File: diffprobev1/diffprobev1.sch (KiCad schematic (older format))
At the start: 36 parts

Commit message: diffprobe sch
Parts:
- added J? (x3): Conn_01x02_Male, symbol Connector:Conn_01x02_Male
- added J? (x2): Conn_01x03_Male, symbol Connector:Conn_01x03_Male
- added unit 3 of U1
- U?: value LF356 -> TL072
- U?: value TL082 -> TL072
- gave numbers to parts that had none: 1
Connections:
- wire segments 0 -> 91
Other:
- moved on the sheet: C?, D?, R?, U1A, U?

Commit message: almost there
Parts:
- removed C? (x2): C, symbol Device:C
- removed C?: CP, symbol Device:CP
- removed J?: Conn_01x02_Male, symbol Connector:Conn_01x02_Male
- removed J?: Conn_01x03_Male, symbol Connector:Conn_01x03_Male
- removed Q?: Q_PNP_EBC, symbol Device:Q_PNP_EBC
- removed R? (x6): R, symbol Device:R
- removed U?: TL072, symbol Amplifier_Operational:LF356
- removed U?: TL072, symbol Amplifier_Operational:TL082
- added C? (x18): C, symbol Device:C
- added C? (x5): CP, symbol Device:CP
- added D? (x4): D_Zener, symbol Device:D_Zener
- added D? (x12): D, symbol Device:D
- added J? (x7): Conn_01x02_Male, symbol Connector:Conn_01x02_Male
- added J?: 8P8C, symbol Connector:8P8C
- added R? (x32): R, symbol Device:R
- added U? (x3): TL071, symbol Amplifier_Operational:TL071
- added U? (x6): TL072, symbol Amplifier_Operational:TL072
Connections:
- net labels added: +15V, -15V, GND1
- wire segments 91 -> 416
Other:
- moved on the sheet: C?, D?, J?, R?, U1A, U1B, U1C

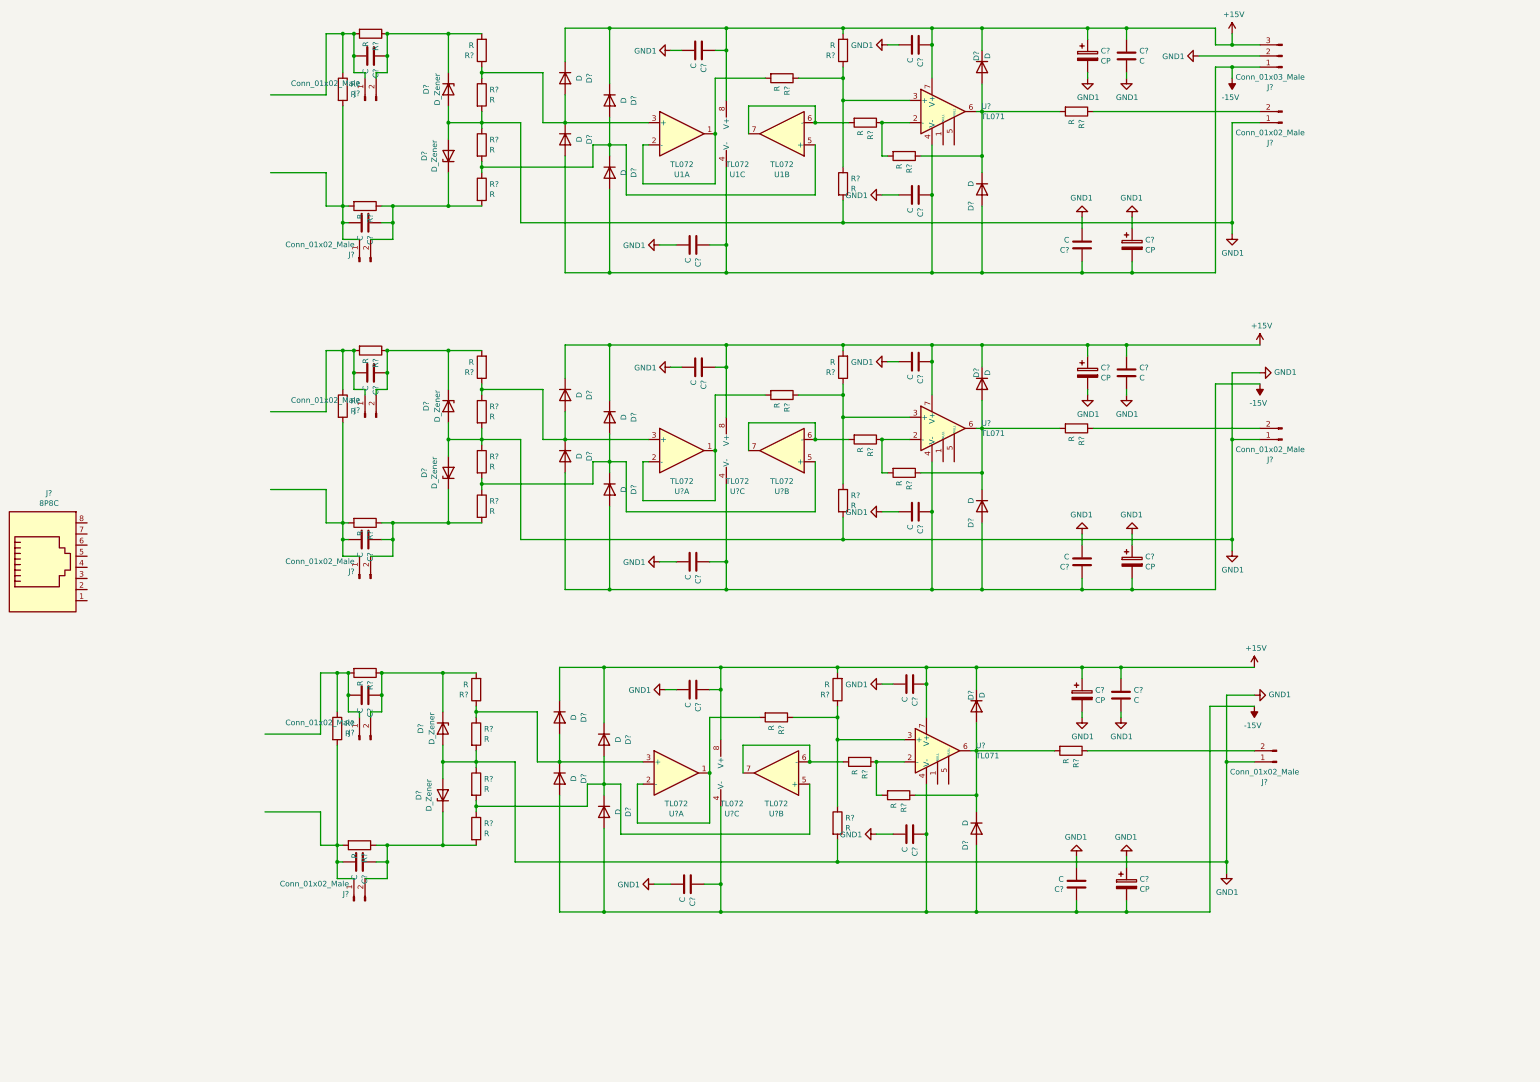
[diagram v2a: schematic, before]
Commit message: diff probe sch progress
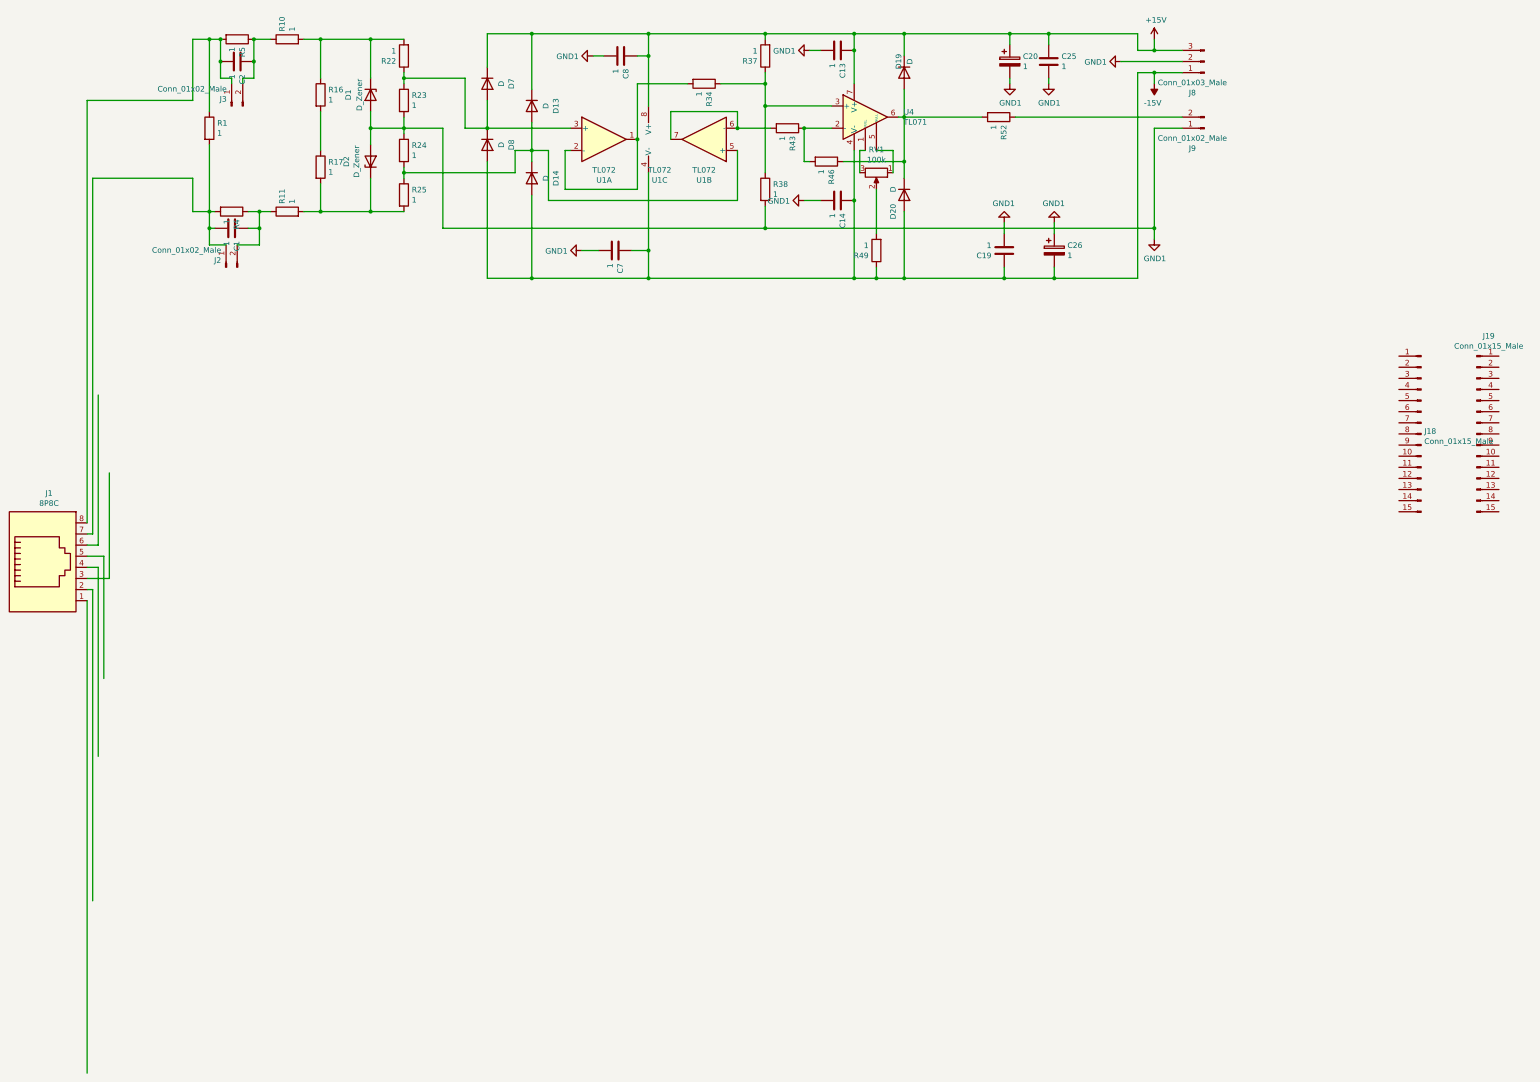
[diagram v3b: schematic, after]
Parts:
- removed C? (x16): C, symbol Device:C
- removed C? (x4): CP, symbol Device:CP
- removed D? (x4): D_Zener, symbol Device:D_Zener
- removed D? (x12): D, symbol Device:D
- removed J? (x6): Conn_01x02_Male, symbol Connector:Conn_01x02_Male
- removed R? (x26): R, symbol Device:R
- removed U? (x6): TL072, symbol Amplifier_Operational:TL072
- removed U? (x2): TL071, symbol Amplifier_Operational:TL071
- added J18, J19: Conn_01x15_Male, symbol Connector:Conn_01x15_Male
- added R10: 1, Capacitor_SMD:C_0805_2012Metric_Pad1.18x1.45mm_HandSolder, symbol Device:R
- added R11, R16, R17, R49: 1, symbol Device:R
- added RV1: 100k, symbol Device:R_POT
- C1, C13, C14, C19, C25, C7, C8: renamed from C?; value C -> 1
- C2: renamed from C?; value C -> 1; footprint (none) -> Capacitor_SMD:C_0805_2012Metric_Pad1.18x1.45mm_HandSolder
- C20, C26: renamed from C?; value CP -> 1
- R1, R4, R5: renamed from R?; value R -> 1; footprint (none) -> Capacitor_SMD:C_0805_2012Metric_Pad1.18x1.45mm_HandSolder
- R22, R23, R24, R25, R34, R37, R38, R43, R46, R52: renamed from R?; value R -> 1
- gave numbers to parts that had none: 14
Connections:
- wire segments 416 -> 170
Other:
- moved on the sheet: C1, C13, C14, C19, C2, C20, C25, C26, C7, C8, D1, D13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

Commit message: sch in progress
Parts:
- added C? (x3): 1, Capacitor_SMD:C_0805_2012Metric_Pad1.18x1.45mm_HandSolder, symbol Device:C
- added C? (x27): 1, symbol Device:C
- added C? (x9): 1, symbol Device:CP
- added D? (x6): D_Zener, symbol Device:D_Zener
- added D? (x27): D, symbol Device:D
- added J? (x6): Conn_01x03_Male, symbol Connector:Conn_01x03_Male
- added J? (x9): Conn_01x02_Male, symbol Connector:Conn_01x02_Male
- added J? (x3): Conn_01x01_Male, symbol Connector:Conn_01x01_Male
- added J?: Conn_01x06_Male, symbol Connector:Conn_01x06_Male
- added Q? (x6): Q_NMOS_GDSD, symbol Device:Q_NMOS_GDSD
- added R? (x54): 1, symbol Device:R
- added R? (x12): 1, Capacitor_SMD:C_0805_2012Metric_Pad1.18x1.45mm_HandSolder, symbol Device:R
- added RV? (x3): 100k, symbol Device:R_POT
- added U? (x9): TL072, symbol Amplifier_Operational:TL072
- added U? (x3): TL071, symbol Amplifier_Operational:TL071
- added U? (x3): IR2101, symbol Driver_FET:IR2101
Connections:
- net labels added: A0, A1, A2, A3, A4, A5, A6, A7
- wire segments 170 -> 716
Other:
- note added: "A0"
- moved on the sheet: J18, J19

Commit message: schematic in progress
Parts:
- removed C? (x6): 1, symbol Device:C
- removed C? (x3): 1, symbol Device:CP
- removed D? (x9): D, symbol Device:D
- removed J8, J? (x3): Conn_01x03_Male, symbol Connector:Conn_01x03_Male
- removed J9, J? (x3): Conn_01x02_Male, symbol Connector:Conn_01x02_Male
- removed J? (x3): Conn_01x01_Male, symbol Connector:Conn_01x01_Male
- removed J?: Conn_01x06_Male, symbol Connector:Conn_01x06_Male
- removed Q? (x6): Q_NMOS_GDSD, symbol Device:Q_NMOS_GDSD
- removed R? (x12): 1, symbol Device:R
- removed U? (x3): IR2101, symbol Driver_FET:IR2101
- added D33, D34: LED, symbol Device:LED
- added J10, J14: Conn_02x10_Odd_Even, symbol Connector_Generic:Conn_02x10_Odd_Even
- added J15: Conn_01x03_Male, symbol Connector:Conn_01x03_Male
- added J16: Conn_01x02_Male, symbol Connector:Conn_01x02_Male
- added J17: 8P8C, symbol Connector:8P8C
- added Q1, Q2: BC107, Package_TO_SOT_THT:TO-18-3, symbol Transistor_BJT:BC107
- added R73, R74, R75, R76: 1, symbol Device:R
- gave numbers to parts that had none: 126
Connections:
- net A0: now also J11.2 (Pin_2)
- net A1: now also J12.2 (Pin_2)
- net A2: now also J13.2 (Pin_2)
- net A3: now also J15.2 (Pin_2); no longer R52.1
- net A4: now also R52.1
- net A5: now also R71.1
- net A6: now also R72.1
- net A7: now also R70.1
- net GND1: now also J11.1 (Pin_1), J12.1 (Pin_1), J13.1 (Pin_1), J18.4 (Pin_4), J19.2 (Pin_2), J14.2 (Pin_2), J15.1 (Pin_1), J16.1 (Pin_1), J17.1, J17.3, J17.5, J17.7, Q1.1 (E), Q2.1 (E)
- net +3V3: now reaches J19.14 (Pin_14)
- net +3V3: now also J10.1 (Pin_1)
- net d13clk: now reaches J19.15 (Pin_15)
- net d13clk: now also J10.13 (Pin_13), J17.6
- net +5V: now reaches J19.4 (Pin_4)
- net +5V: now also J11.3 (Pin_3), J12.3 (Pin_3), J13.3 (Pin_3), J15.3 (Pin_3), J16.2 (Pin_2), R74.2, R76.2
- net d7: now reaches J18.10 (Pin_10)
- net d7: now also R73.2
- net d8: now reaches J18.11 (Pin_11)
- net d8: now also R75.2
- net d9_1a: now reaches J18.12 (Pin_12)
- net d9_1a: now also J14.9 (Pin_9)
- net d10_1b: now reaches J18.13 (Pin_13)
- net d11mosi_2a: now reaches J18.14 (Pin_14)
- net d11mosi_2a: now also J14.12 (Pin_12), J17.2
- net d12miso: now reaches J18.15 (Pin_15)
- net d12miso: now also J14.14 (Pin_14), J17.4
- net d2_enDRV: now reaches J18.5 (Pin_5)
- net d2_enDRV: now also J14.16 (Pin_16)
- net d3_2b: now reaches J18.6 (Pin_6)
- net d4_cs_pos: now reaches J18.7 (Pin_7)
- net d4_cs_pos: now also J17.8
- net d5_0a: now reaches J18.8 (Pin_8)
- net d5_0a: now also J14.1 (Pin_1)
- net d6_0b: now reaches J18.9 (Pin_9)
- net d6_0b: now also J14.5 (Pin_5)
- new net: Q1.2 (B), R73.1
- new net: D33.1 (K), Q1.3 (C)
- new net: Q2.2 (B), R75.1
- new net: D34.1 (K), Q2.3 (C)
- new net: D33.2 (A), R74.1
- new net: D34.2 (A), R76.1
- new net cs: J14.4 (Pin_4)
- no-connect marks 0 -> 37
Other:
- note added: "-pwm t0a t0b t1a\n-interrupt\na0 a1 a2 pos tx tx tx tx rx t2a \na0 a1 a3 pos tx tx tx tx rx t2a \na0 a1 a4 pos tx tx tx tx rx t2a \n.\n.\n.\n\n-loop: \nprotection\ncurrent loop, \n clark, \n park, \n pid, \n input torque from rx\n"
- moved on the sheet: J11, J12, J13, J18, J19
